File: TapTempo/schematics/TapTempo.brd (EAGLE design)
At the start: 60.6 x 50.3 mm, 46 parts, among them IC1 MEGA168, IC2 MCP4921, IC3 TL072D, IC4 LM4041A12DBZ, Q301 BC846, Q701 BC846, Y1 16Mhz

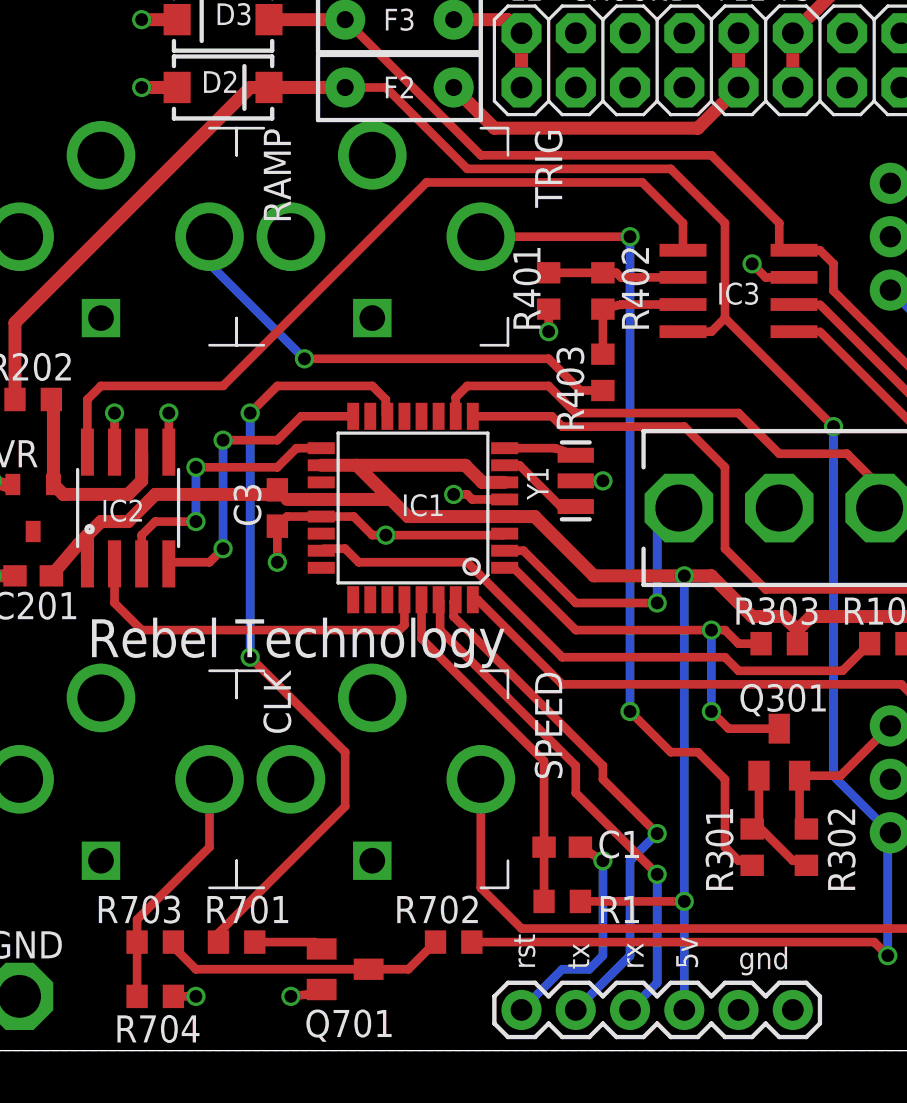
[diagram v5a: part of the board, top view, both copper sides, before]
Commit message: TapTempo Rev01 ordered from Seeed studios
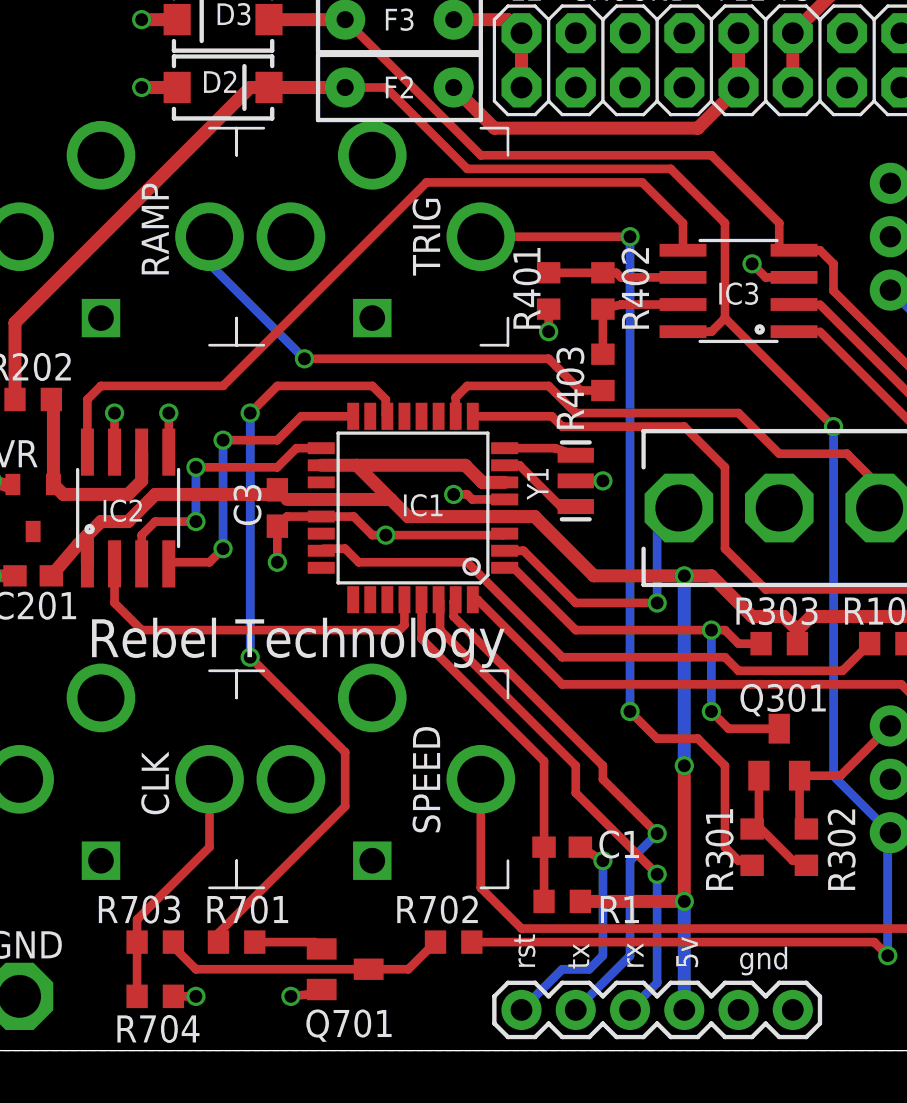
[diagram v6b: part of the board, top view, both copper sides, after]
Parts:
- added U$1: (no value), Rebel:RT-LOGO-REBEL-BL
- added U$3: (no value), Rebel:RT-LOGO-TECH-BL
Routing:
- net +5V: vias 2 -> 3
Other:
- board text added: "-12v"
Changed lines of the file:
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@@
 <text x="38.735" y="50.165" size="1.016" layer="21" font="vector" align="top-center">+5</text>
 <text x="31.115" y="50.165" size="1.016" layer="21" font="vector" align="top-center">GROUND</text>
-<text x="23.495" y="46.355" size="1.016" layer="30" font="vector" rot="MR270" align="center">-12</text>
-<text x="34.29" y="40.64" size="1.016" layer="30" font="vector" rot="MR180" align="center">Rebel Technology</text>
+<text x="26.035" y="49.53" size="1.016" layer="30" font="vector" rot="MR180" align="center">-12v</text>
 <wire x1="60.63" y1="0" x2="0" y2="0" width="0" layer="20"/>
 <text x="1.27" y="27.305" size="1.27" layer="25" font="vector">VR</text>
@@
 <attribute name="VALUE" x="27.813" y="32.639" size="1.27" layer="27" rot="R270"/>
 </element>
-<element name="SPEED" library="TomW" package="PJ-301B" value="PJ-301B" x="19.05" y="12.7" rot="R270"/>
+<element name="SPEED" library="TomW" package="PJ-301B" value="PJ-301B" x="19.05" y="12.7" smashed="yes" rot="R270">
+<attribute name="NAME" x="20.955" y="15.24" size="1.27" layer="25" rot="R270"/>
+<attribute name="VALUE" x="10.16" y="17.78" size="1.27" layer="27" rot="R270"/>
+</element>
 <element name="TRIG" library="TomW" package="PJ-301B" value="PJ-301B" x="19.05" y="38.1" smashed="yes" rot="R270">
-<attribute name="NAME" x="26.67" y="43.18" size="1.27" layer="25" rot="R270"/>
+<attribute name="NAME" x="20.955" y="40.005" size="1.27" layer="25" rot="R270"/>
 <attribute name="VALUE" x="10.16" y="43.18" size="1.27" layer="27" rot="R270"/>
 </element>
 <element name="RAMP" library="TomW" package="PJ-301B" value="PJ-301B" x="6.35" y="38.1" smashed="yes" rot="R270">
-<attribute name="NAME" x="13.97" y="43.18" size="1.27" layer="25" rot="R270"/>
+<attribute name="NAME" x="8.255" y="40.64" size="1.27" layer="25" rot="R270"/>
 <attribute name="VALUE" x="-2.54" y="43.18" size="1.27" layer="27" rot="R270"/>
 </element>
-<element name="CLK" library="TomW" package="PJ-301B" value="PJ-301B" x="6.35" y="12.7" rot="R270"/>
+<element name="CLK" library="TomW" package="PJ-301B" value="PJ-301B" x="6.35" y="12.7" smashed="yes" rot="R270">
+<attribute name="NAME" x="8.255" y="13.97" size="1.27" layer="25" rot="R270"/>
+<attribute name="VALUE" x="-2.54" y="17.78" size="1.27" layer="27" rot="R270"/>
+</element>
 <element name="IC2" library="Rebel" package="SOIC8" value="MCP4921" x="7.62" y="25.4" smashed="yes">
 <attribute name="VALUE" x="6.35" y="24.765" size="0.4064" layer="27"/>
@@
 <attribute name="VALUE" x="55.499" y="32.512" size="1.27" layer="27" rot="R180"/>
 </element>
+<element name="U$1" library="Rebel" package="RT-LOGO-REBEL-BL" value="" x="54.61" y="19.05" rot="R270"/>
+<element name="U$3" library="Rebel" package="RT-LOGO-TECH-BL" value="" x="54.61" y="40.005" rot="R270"/>
 </elements>
 <signals>
@@
 <wire x1="57.15" y1="41.665" x2="52.705" y2="46.11" width="0.6096" layer="1"/>
 <wire x1="57.15" y1="26.67" x2="57.15" y2="41.665" width="0.6096" layer="1"/>
-<wire x1="33.655" y1="1.905" x2="33.655" y2="6.985" width="0.4064" layer="16"/>
+<wire x1="33.655" y1="1.905" x2="33.655" y2="6.985" width="0.6096" layer="16"/>
 <via x="33.655" y="22.225" extent="1-16" drill="0.6" shape="square"/>
-<wire x1="33.655" y1="6.985" x2="33.655" y2="22.225" width="0.4064" layer="16"/>
 <wire x1="26.65" y1="25" x2="29.425" y2="22.225" width="0.6096" layer="1"/>
 <via x="33.655" y="6.985" extent="1-16" drill="0.6" shape="square"/>
@@
 <wire x1="4.025" y1="22.225" x2="5.295" y2="23.71" width="0.6096" layer="1"/>
 <wire x1="5.295" y1="23.71" x2="5.715" y2="24.13" width="0.6096" layer="1"/>
-<wire x1="33.655" y1="6.985" x2="28.79" y2="6.985" width="0.4064" layer="1"/>
+<wire x1="33.655" y1="6.985" x2="28.79" y2="6.985" width="0.6096" layer="1"/>
 <wire x1="38.95" y1="19.05" x2="38.95" y2="19.685" width="0.6096" layer="1"/>
 <wire x1="38.95" y1="19.685" x2="39.585" y2="20.32" width="0.6096" layer="1"/>
 <wire x1="36.83" y1="20.32" x2="38.315" y2="20.32" width="0.6096" layer="1"/>
 <wire x1="38.315" y1="20.32" x2="38.95" y2="19.685" width="0.6096" layer="1"/>
+<wire x1="33.655" y1="22.225" x2="33.655" y2="13.335" width="0.6096" layer="16"/>
+<via x="33.655" y="13.335" extent="1-16" drill="0.6" shape="square"/>
+<wire x1="33.655" y1="13.335" x2="33.655" y2="6.985" width="0.6096" layer="1"/>
 </signal>
 <signal name="DELIN">
@@
 <signal name="STOPSW">
 <contactref element="S1" pad="3"/>
-<wire x1="32.385" y1="20.955" x2="32.385" y2="24.384" width="0.4064" layer="16"/>
-<wire x1="32.385" y1="24.384" x2="33.401" y2="25.4" width="0.4064" layer="16"/>
 <contactref element="IC1" pad="2"/>
 <wire x1="25.2476" y1="23.4" x2="26.13" y2="23.4" width="0.4064" layer="1"/>
@@
 <wire x1="28.575" y1="20.955" x2="32.385" y2="20.955" width="0.4064" layer="1"/>
 <via x="32.385" y="20.955" extent="1-16" drill="0.6" shape="square"/>
+<wire x1="33.401" y1="25.4" x2="33.02" y2="25.4" width="0.4064" layer="16"/>
+<wire x1="33.02" y1="25.4" x2="32.385" y2="24.765" width="0.4064" layer="16"/>
+<wire x1="32.385" y1="24.765" x2="32.385" y2="20.955" width="0.4064" layer="16"/>
 </signal>
 <signal name="ALTA">
@@
 <wire x1="31.115" y1="38.1" x2="31.115" y2="15.875" width="0.4064" layer="16"/>
 <via x="31.115" y="15.875" extent="1-16" drill="0.6" shape="square"/>
-<wire x1="34.29" y1="13.97" x2="35.56" y2="12.7" width="0.4064" layer="1"/>
-<wire x1="35.56" y1="12.7" x2="35.56" y2="9.525" width="0.4064" layer="1"/>
+<wire x1="34.29" y1="14.605" x2="35.56" y2="13.335" width="0.4064" layer="1"/>
+<wire x1="35.56" y1="13.335" x2="35.56" y2="9.525" width="0.4064" layer="1"/>
 <wire x1="35.56" y1="9.525" x2="36.195" y2="8.89" width="0.4064" layer="1"/>
 <wire x1="36.195" y1="8.89" x2="36.615" y2="8.89" width="0.4064" layer="1"/>
 <wire x1="36.615" y1="8.89" x2="36.83" y2="8.675" width="0.4064" layer="1"/>
-<wire x1="34.29" y1="13.97" x2="33.02" y2="13.97" width="0.4064" layer="1"/>
-<wire x1="33.02" y1="13.97" x2="31.115" y2="15.875" width="0.4064" layer="1"/>
+<wire x1="34.29" y1="14.605" x2="32.385" y2="14.605" width="0.4064" layer="1"/>
+<wire x1="32.385" y1="14.605" x2="31.115" y2="15.875" width="0.4064" layer="1"/>
 </signal>
 <signal name="N$44">

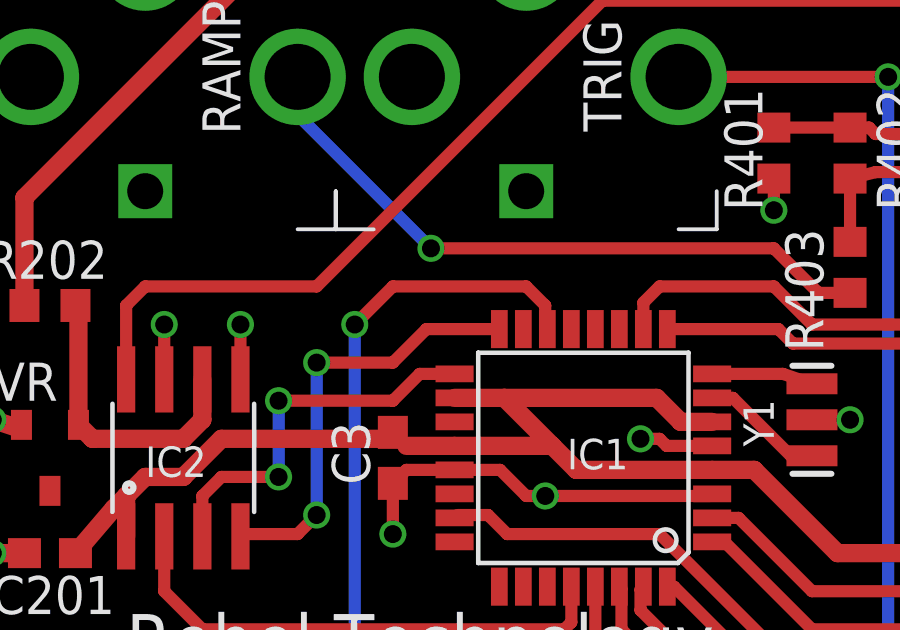
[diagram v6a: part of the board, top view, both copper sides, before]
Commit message: fixed error; SDI connect to MOSI instead of MISO
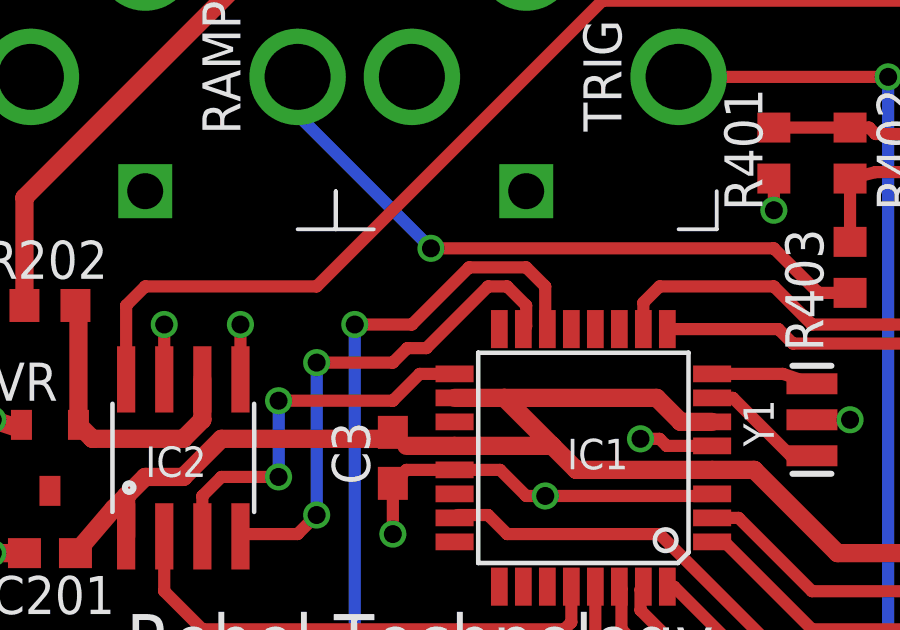
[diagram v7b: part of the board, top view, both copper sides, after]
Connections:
- net CLKOUT renamed TRIGOUT
- removed net DELOUT: IC1.13
- removed net DIVOUT: IC1.12
- removed net MODEB: IC1.11
- removed net SW1: BUTTON.1, IC1.32
- new net GATEIN: IC1.1, Q301.3, R303.2
- net SDI: now also IC1.15; no longer IC1.16
- net TRIGIN: now also BUTTON.1, IC1.32; no longer IC1.1, Q301.3, R303.2
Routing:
- net SW1: track 42.0 -> 0.00 mm
- net TRIGIN: track 20.8 -> 42.0 mm, vias 2 -> 0
- net GATEIN: track 0.00 -> 20.8 mm, vias 0 -> 2
- net SDI: track 14.6 -> 17.2 mm
- net TRIGOUT: track 37.0 -> 37.9 mm
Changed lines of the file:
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@@
 <wire x1="20.555" y1="19.92" x2="20.32" y2="19.685" width="0.4064" layer="1"/>
 </signal>
-<signal name="TRIGIN">
+<signal name="GATEIN">
 <contactref element="IC1" pad="1"/>
 <contactref element="Q301" pad="3"/>
@@
 <wire x1="20.74" y1="3.81" x2="22.01" y2="5.08" width="0.4064" layer="1"/>
 </signal>
-<signal name="DIVOUT">
-<contactref element="IC1" pad="12"/>
-</signal>
-<signal name="DELOUT">
-<contactref element="IC1" pad="13"/>
-</signal>
-<signal name="CLKOUT">
+<signal name="TRIGOUT">
 <contactref element="R701" pad="1"/>
 <contactref element="IC1" pad="14"/>
@@
 <wire x1="13.335" y1="18.415" x2="13.335" y2="29.845" width="0.4064" layer="16"/>
 <via x="13.335" y="29.845" extent="1-16" drill="0.6" shape="square"/>
-<wire x1="13.335" y1="29.845" x2="14.605" y2="31.115" width="0.4064" layer="1"/>
-<wire x1="14.605" y1="31.115" x2="19.05" y2="31.115" width="0.4064" layer="1"/>
-<wire x1="19.05" y1="31.115" x2="19.685" y2="30.48" width="0.4064" layer="1"/>
-<wire x1="19.685" y1="30.48" x2="19.685" y2="29.7626" width="0.4064" layer="1"/>
+<wire x1="13.335" y1="29.845" x2="15.24" y2="29.845" width="0.4064" layer="1"/>
+<wire x1="15.24" y1="29.845" x2="17.145" y2="31.75" width="0.4064" layer="1"/>
+<wire x1="17.145" y1="31.75" x2="19.05" y2="31.75" width="0.4064" layer="1"/>
+<wire x1="19.05" y1="31.75" x2="19.685" y2="31.115" width="0.4064" layer="1"/>
+<wire x1="19.685" y1="31.115" x2="19.685" y2="29.7626" width="0.4064" layer="1"/>
 <wire x1="19.685" y1="29.7626" x2="19.755" y2="29.6926" width="0.4064" layer="1"/>
 </signal>
@@
 <wire x1="27.09" y1="6.985" x2="27.09" y2="9.525" width="0.4064" layer="1"/>
 <wire x1="27.09" y1="9.525" x2="27.09" y2="13.55" width="0.4064" layer="1"/>
-</signal>
-<signal name="MODEB">
-<contactref element="IC1" pad="11"/>
 </signal>
 <signal name="MODESW">
@@
 <wire x1="58.42" y1="27.305" x2="59.055" y2="26.67" width="0.4064" layer="16"/>
 </signal>
-<signal name="SW1">
+<signal name="TRIGIN">
 <contactref element="BUTTON" pad="1"/>
 <contactref element="IC1" pad="32"/>
@@
 <signal name="SDI">
 <contactref element="IC2" pad="4"/>
-<contactref element="IC1" pad="16"/>
-<wire x1="18.155" y1="29.6926" x2="15.7226" y2="29.6926" width="0.4064" layer="1"/>
-<wire x1="15.7226" y1="29.6926" x2="14.605" y2="28.575" width="0.4064" layer="1"/>
+<wire x1="15.0876" y1="29.0576" x2="14.605" y2="28.575" width="0.4064" layer="1"/>
 <wire x1="14.605" y1="28.575" x2="12.065" y2="28.575" width="0.4064" layer="1"/>
 <via x="12.065" y="28.575" extent="1-16" drill="0.6" shape="square"/>
@@
 <wire x1="9.4488" y1="22.86" x2="11.43" y2="22.86" width="0.4064" layer="1"/>
 <wire x1="11.43" y1="22.86" x2="12.065" y2="23.495" width="0.4064" layer="1"/>
+<contactref element="IC1" pad="15"/>
+<wire x1="15.0876" y1="29.0576" x2="15.7226" y2="29.0576" width="0.4064" layer="1"/>
+<wire x1="15.7226" y1="29.0576" x2="17.78" y2="31.115" width="0.4064" layer="1"/>
+<wire x1="17.78" y1="31.115" x2="18.415" y2="31.115" width="0.4064" layer="1"/>
+<wire x1="18.415" y1="31.115" x2="19.05" y2="30.48" width="0.4064" layer="1"/>
+<wire x1="19.05" y1="30.48" x2="19.05" y2="29.7876" width="0.4064" layer="1"/>
+<wire x1="19.05" y1="29.7876" x2="18.955" y2="29.6926" width="0.4064" layer="1"/>
 </signal>
 <signal name="SCK">
